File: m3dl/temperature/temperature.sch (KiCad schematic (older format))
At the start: 60 parts

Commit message: Completed all Schematics
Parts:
- removed C? (x9): 10n, symbol C_Small
- removed C? (x9): 1n, symbol C_Small
- removed J?: NORTH TOP, agg:TFML-110-02-L-D, symbol CONN_02x10
- removed J?: NORTH BOT, agg:SFML-110-02-L-D-LC, symbol CONN_02x10
- added J?: NORTH TOP, agg:TFML-110-02-L-D, symbol CONN_02x10
- added J?: NORTH BOT, agg:SFML-110-02-L-D-LC, symbol CONN_02x10
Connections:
- net CH1+: now also IC?.17 (CH2); no longer IC?.16 (CH1)
- net CH2+: now also IC?.19 (CH4); no longer IC?.18 (CH3)
- net CH3+: now also IC?.21 (CH6); no longer IC?.20 (CH5)
- net CH4+: now also IC?.23 (CH8); no longer IC?.22 (CH7)
- net CH5+: now also IC?.25 (CH10); no longer IC?.24 (CH9)
- net CH6+: now also IC?.27 (CH12); no longer IC?.26 (CH11)
- net CH7+: now also IC?.29 (CH14); no longer IC?.28 (CH13)
- net CH8+: now also IC?.31 (CH16); no longer IC?.30 (CH15)
- net CH9+: now also IC?.33 (CH18); no longer IC?.32 (CH17)
- net GND: now also IC?.16 (CH1), IC?.18 (CH3), IC?.20 (CH5), IC?.22 (CH7), IC?.24 (CH9), IC?.26 (CH11), IC?.28 (CH13), IC?.30 (CH15), IC?.32 (CH17), R?.1, R?.1, R?.1, R?.1, R?.1, R?.1, R?.1, R?.1, R?.1, J?.1, J?.1, J?.19, J?.19, J?.2, J?.2, J?.20, J?.20
- net PRESSURE1: now also J?.16, J?.16
- net PRESSURE2: now also J?.18, J?.18
- net PRESSURE3: now also J?.17, J?.17
- net SPI1_CS: now also J?.3, J?.3
- net SPI1_MISO: now also J?.13, J?.13
- net SPI1_MOSI: now also J?.11, J?.11
- net SPI1_SCK: now also J?.15, J?.15
- net STRAIN1: now also J?.4, J?.4
- net STRAIN2: now also J?.6, J?.6
- net STRAIN3: now also J?.8, J?.8
- net STRAIN4: now also J?.10, J?.10
- net STRAIN5: now also J?.12, J?.12
- net STRAIN6: now also J?.14, J?.14
- net TEMP_INT: now also J?.5, J?.5
- removed net CH1-: IC?.17 (CH2), R?.1
- removed net CH2-: IC?.19 (CH4), R?.1
- removed net CH3-: IC?.21 (CH6), R?.1
- removed net CH4-: IC?.23 (CH8), R?.1
- removed net CH5-: IC?.25 (CH10), R?.1
- removed net CH6-: IC?.27 (CH12), R?.1
- removed net CH7-: IC?.29 (CH14), R?.1
- removed net CH8-: IC?.31 (CH16), R?.1
- removed net CH9-: IC?.33 (CH18), R?.1
- new net PRESSURE4: J?.9, J?.9
- new net PRESSURE5: J?.7, J?.7
- no-connect marks 2 -> 1

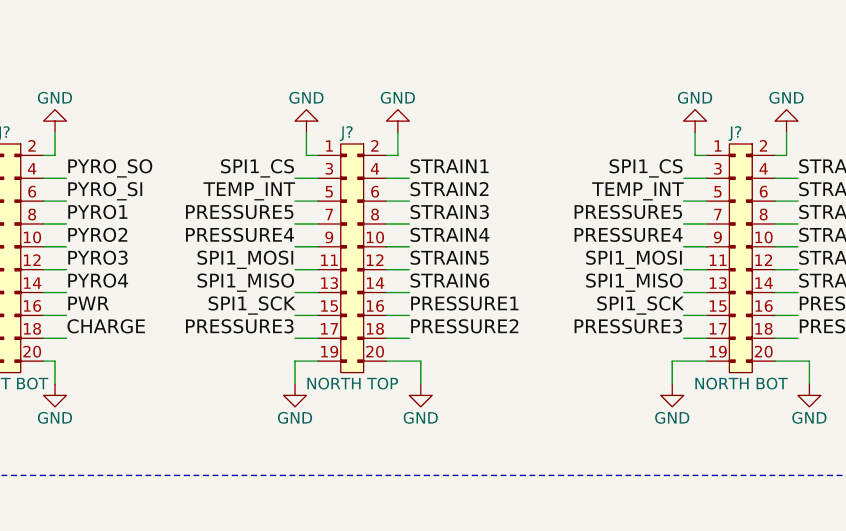
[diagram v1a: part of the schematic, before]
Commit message: Modified South Pin Header Layout
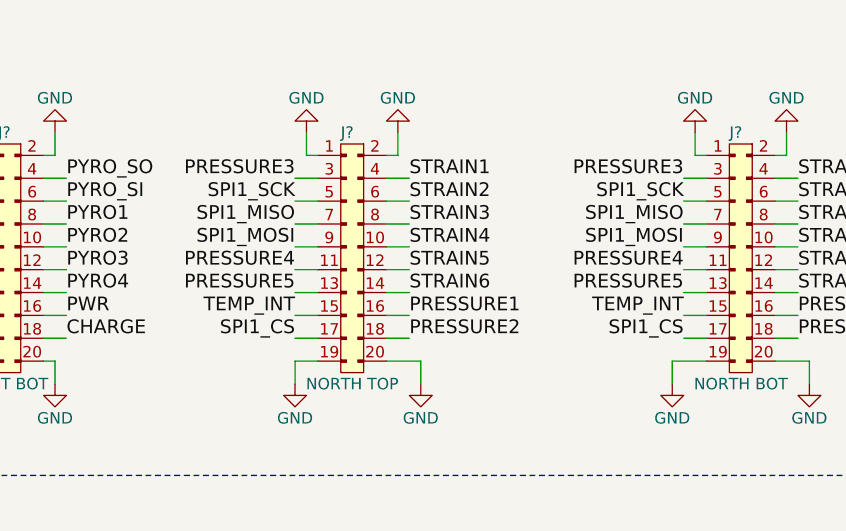
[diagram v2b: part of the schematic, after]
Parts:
- removed J?: NORTH TOP, agg:TFML-110-02-L-D, symbol CONN_02x10
- removed J?: NORTH BOT, agg:SFML-110-02-L-D-LC, symbol CONN_02x10
- added J?: NORTH TOP, agg:TFML-110-02-L-D, symbol CONN_02x10
- added J?: NORTH BOT, agg:SFML-110-02-L-D-LC, symbol CONN_02x10
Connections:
- net GND: now also J?.1, J?.1, J?.19, J?.19, J?.2, J?.2, J?.20, J?.20
- net PRESSURE1: now also J?.16, J?.16
- net PRESSURE2: now also J?.18, J?.18
- net PRESSURE3: now also J?.3, J?.3
- net PRESSURE4: now also J?.11, J?.11
- net PRESSURE5: now also J?.13, J?.13
- net SPI1_CS: now also J?.17, J?.17
- net SPI1_MISO: now also J?.7, J?.7
- net SPI1_MOSI: now also J?.9, J?.9
- net SPI1_SCK: now also J?.5, J?.5
- net STRAIN1: now also J?.4, J?.4
- net STRAIN2: now also J?.6, J?.6
- net STRAIN3: now also J?.8, J?.8
- net STRAIN4: now also J?.10, J?.10
- net STRAIN5: now also J?.12, J?.12
- net STRAIN6: now also J?.14, J?.14
- net TEMP_INT: now also J?.15, J?.15

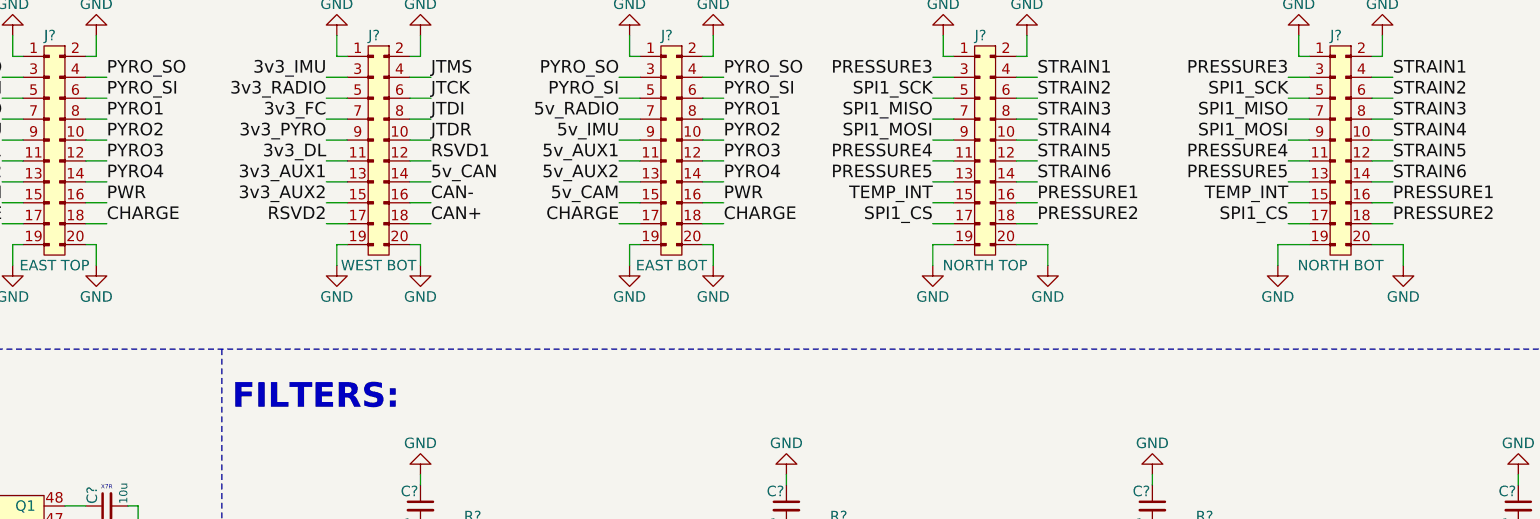
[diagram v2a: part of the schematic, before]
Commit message: Finished routing Pressure PCB - Needs Silkscreen
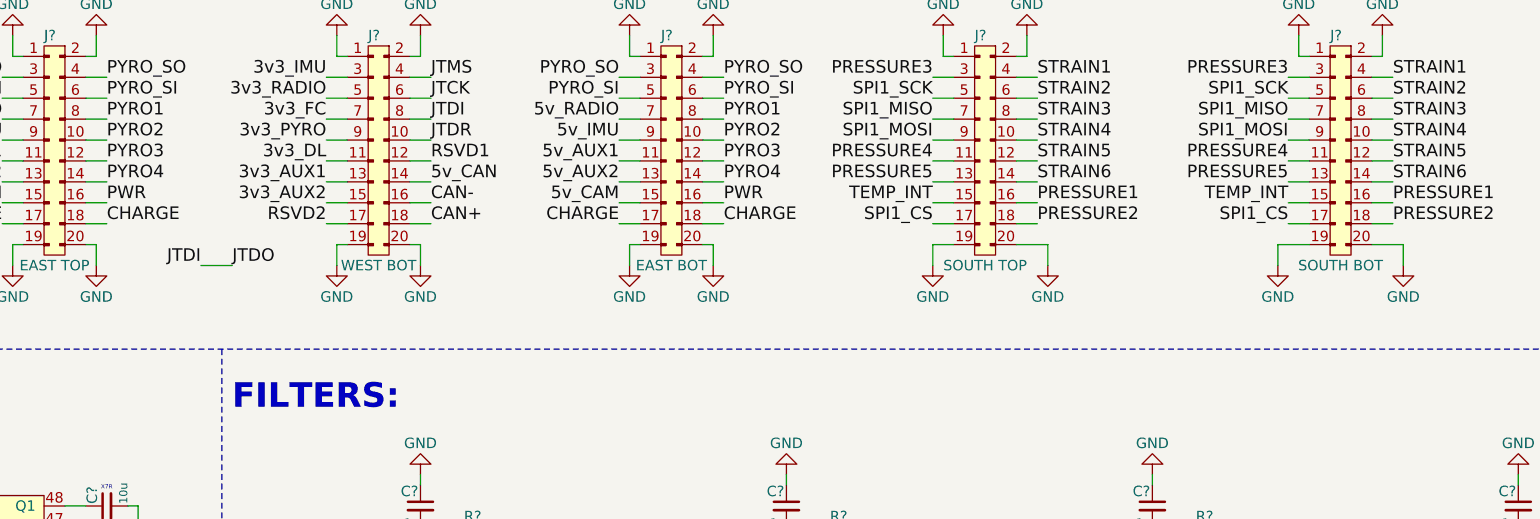
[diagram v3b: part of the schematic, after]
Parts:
- J?: value NORTH TOP -> SOUTH TOP
- J?: value NORTH BOT -> SOUTH BOT
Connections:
- net JTDO is gone; now on net JTDI: J?.8
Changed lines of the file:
@@
 P 7250 1200
 F 0 "J?" H 7150 1300 50  0000 L CNN
-F 1 "NORTH TOP" H 7200 200 50  0000 C CNN
+F 1 "SOUTH TOP" H 7200 200 50  0000 C CNN
 F 2 "agg:TFML-110-02-L-D" H 7250 1200 50  0001 C CNN
 F 3 "" H 7250 1200 50  0001 C CNN
@@
 P 8950 1200
 F 0 "J?" H 8850 1300 50  0000 L CNN
-F 1 "NORTH BOT" H 8900 200 50  0000 C CNN
+F 1 "SOUTH BOT" H 8900 200 50  0000 C CNN
 F 2 "agg:SFML-110-02-L-D-LC" H 8950 1200 50  0001 C CNN
 F 3 "" H 8950 1200 50  0001 C CNN
@@
 Text Label 6950 1800 2    60   ~ 0
 PRESSURE5
+Text Label 3600 2200 0    60   ~ 0
+JTDO
+Text Label 3450 2200 2    60   ~ 0
+JTDI
+Wire Wire Line
+	3450 2200 3600 2200
 $EndSCHEMATC

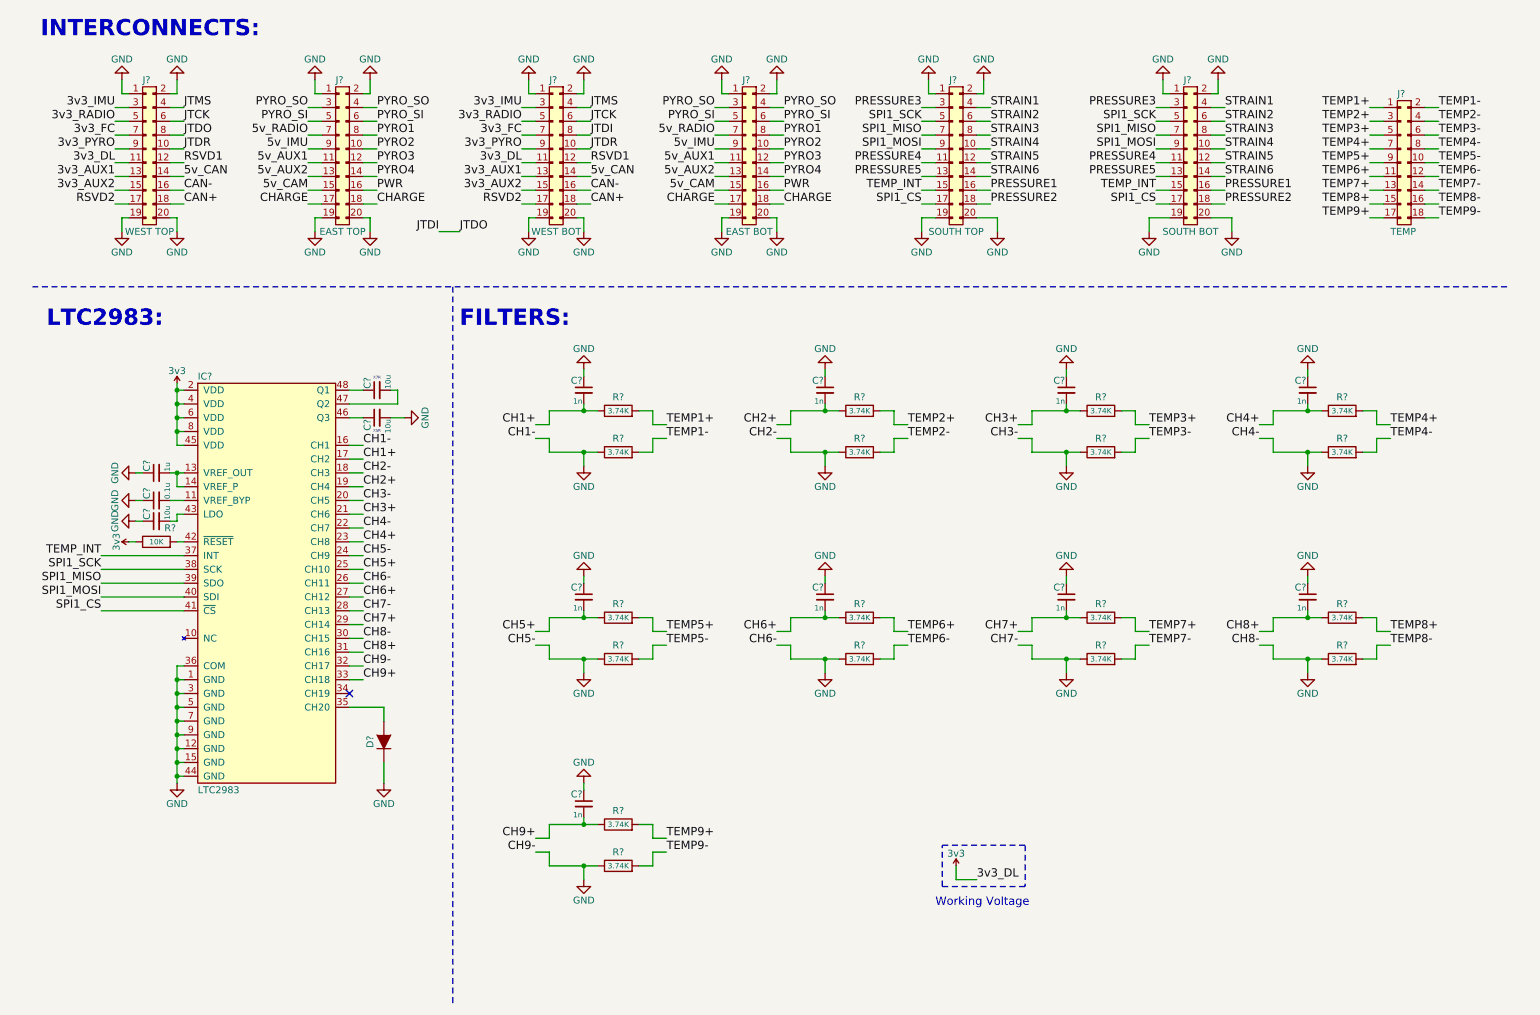
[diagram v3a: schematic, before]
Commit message: Finished Routing Temperature Board - Needs Silkscreen
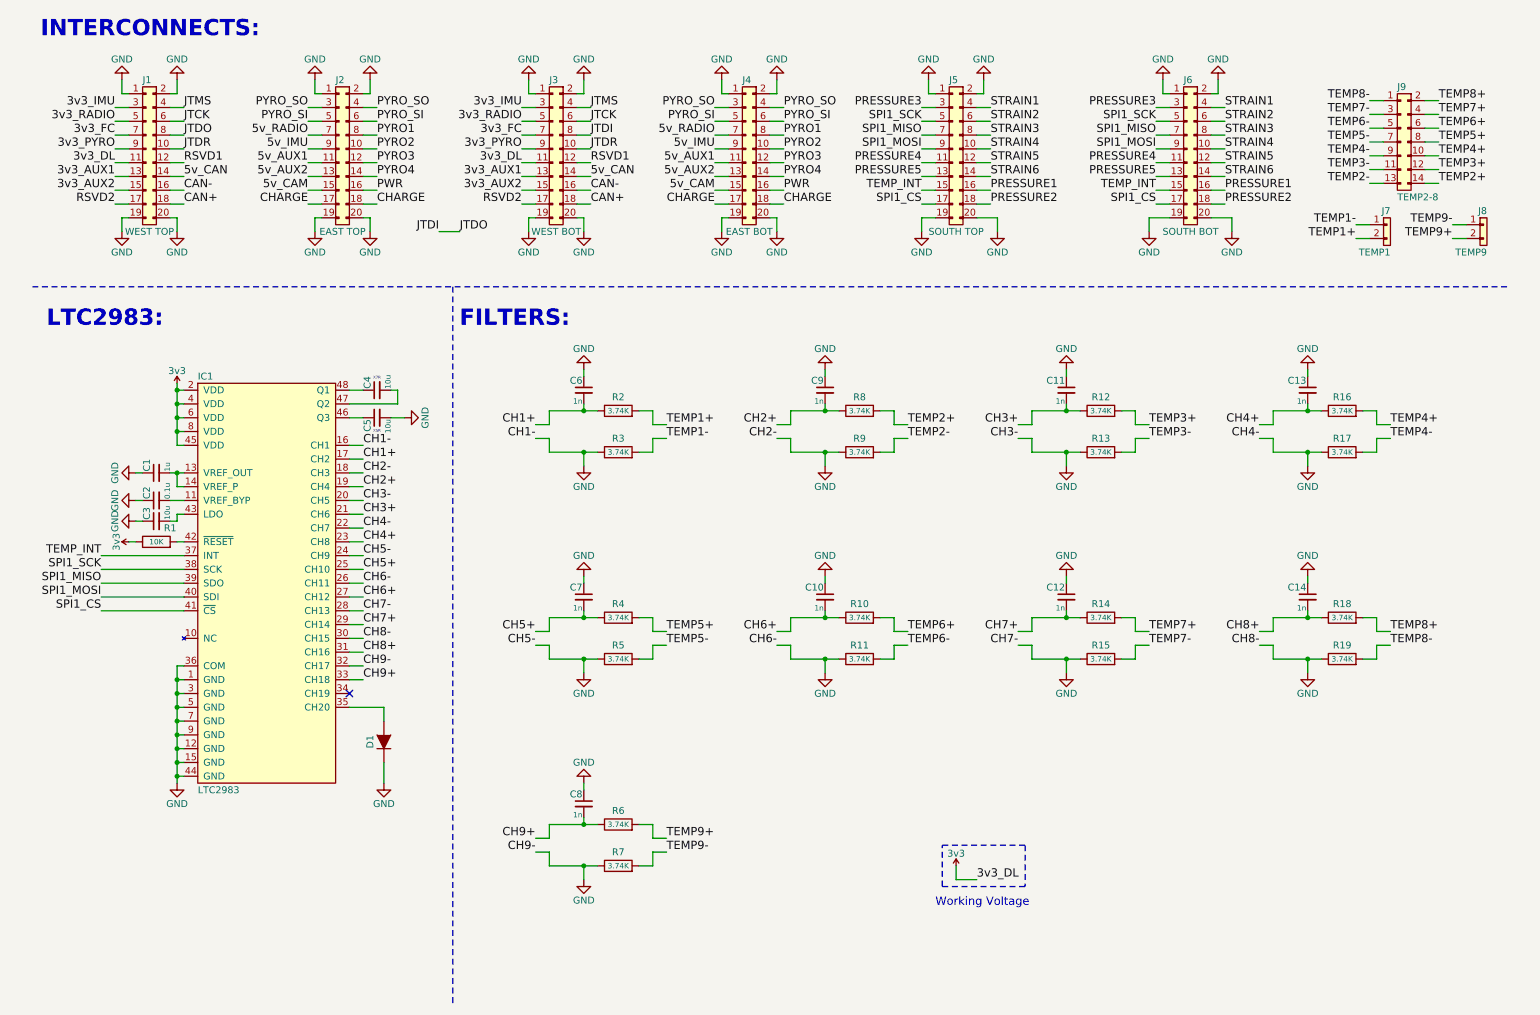
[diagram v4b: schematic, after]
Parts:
- removed J?: TEMP, symbol CONN_02x09
- added J7: TEMP1, Connectors_Molex:Connector_Molex_PicoBlade_53048-0210, symbol CONN_01x02
- added J8: TEMP9, Connectors_Molex:Connector_Molex_PicoBlade_53048-0210, symbol CONN_01x02
- added J9: TEMP2-8, Connectors_Molex:Connector_Molex_PicoBlade_53048-1410, symbol CONN_02x07
- C1, C10, C11, C12, C13, C14, C2, C3, C4, C5, C6, C7, C8, C9: renamed from C?; footprint (none) -> Capacitors_SMD:C_0603
- D1: renamed from D?; footprint (none) -> Diodes_SMD:SOD-123
- IC1: renamed from IC?; footprint LQFP-48 -> agg:LQFP-48
- R1, R10, R11, R12, R13, R14, R15, R16, R17, R18, R19, R2, R3, R4, R5, R6, R7, R8, R9: renamed from R?; footprint (none) -> Resistors_SMD:R_0603
- gave numbers to parts that had none: 6
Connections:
- net TEMP1+: now also J7.2
- net TEMP1-: now also J7.1
- net TEMP2+: now also J9.14
- net TEMP2-: now also J9.13
- net TEMP3+: now also J9.12
- net TEMP3-: now also J9.11
- net TEMP4+: now also J9.10
- net TEMP4-: now also J9.9
- net TEMP5+: now also J9.8
- net TEMP5-: now also J9.7
- net TEMP6+: now also J9.6
- net TEMP6-: now also J9.5
- net TEMP7+: now also J9.4
- net TEMP7-: now also J9.3
- net TEMP8+: now also J9.2
- net TEMP8-: now also J9.1
- net TEMP9+: now also J8.2
- net TEMP9-: now also J8.1

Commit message: Modifications as per review document
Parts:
- added C15: 100n, Capacitors_SMD:C_0603, symbol C_Small
- C2: value 0.1u -> 100n
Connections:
- net 3v3: now also C15.1
- net GND: now also C15.2

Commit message: Compiled BOM
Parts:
- C1: Farnell (none) -> 1865556
- C10, C11, C12, C13, C14, C6, C7, C8, C9: Farnell (none) -> 1813443
- C15, C2: Farnell (none) -> 2496834
- C3, C5: Farnell (none) -> 2211164
- C4: footprint Capacitors_SMD:C_0603 -> agg:0805; Farnell (none) -> 1657936
- D1: Farnell (none) -> 1773476
- J7, J8: Farnell (none) -> 1012259
- J9: Farnell (none) -> 614890
- R1: Farnell (none) -> 9238603
- R10, R11, R12, R13, R14, R15, R16, R17, R18, R19, R2, R3, R4, R5, R6, R7, R8, R9: Farnell (none) -> 2059366

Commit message: Final Tweaks before manufacture
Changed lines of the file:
@@
 L 3v3 #PWR017
 U 1 1 56B8C45F
-P 10600 6800
-F 0 "#PWR017" H 10600 6910 50  0001 L CNN
-F 1 "3v3" H 10600 6890 50  0000 C CNN
-F 2 "" H 10600 6800 60  0000 C CNN
-F 3 "" H 10600 6800 60  0000 C CNN
-	1    10600 6800
+P 10400 6800
+F 0 "#PWR017" H 10400 6910 50  0001 L CNN
+F 1 "3v3" H 10400 6890 50  0000 C CNN
+F 2 "" H 10400 6800 60  0000 C CNN
+F 3 "" H 10400 6800 60  0000 C CNN
+	1    10400 6800
 	1    0    0    -1
 $EndComp
 Text Label 10750 6900 0    60   ~ 0
 3v3_DL
-Text Notes 10450 7100 0    60   ~ 0
+Text Notes 10350 7100 0    60   ~ 0
 Working Voltage
 $Comp
@@
 Connection ~ 1550 5550
 Wire Wire Line
-	1600 5550 1550 5550
+	1550 5550 1600 5550
 Connection ~ 1550 5650
 Wire Wire Line
-	1600 5650 1550 5650
+	1550 5650 1600 5650
 Connection ~ 1550 5750
 Wire Wire Line
-	1600 5750 1550 5750
+	1550 5750 1600 5750
 Connection ~ 1550 5850
 Wire Wire Line
-	1600 5850 1550 5850
+	1550 5850 1600 5850
 Connection ~ 1550 5950
 Wire Wire Line
-	1600 5950 1550 5950
+	1550 5950 1600 5950
 Connection ~ 1550 6050
 Wire Wire Line
-	1600 6050 1550 6050
+	1550 6050 1600 6050
 Connection ~ 1550 6150
-Wire Wire Line
-	1500 6150 1600 6150
 Wire Wire Line
 	1550 5350 1550 6200
@@
 Connection ~ 1550 3350
 Wire Wire Line
-	1500 3350 1600 3350
+	1550 3350 1600 3350
 Connection ~ 1550 3450
 Wire Wire Line
@@
 Connection ~ 1550 3550
 Wire Wire Line
-	1600 3550 1550 3550
+	1550 3550 1600 3550
 Connection ~ 1550 3650
 Wire Wire Line
-	1600 3650 1550 3650
+	1550 3650 1600 3650
 Wire Wire Line
 	1550 3750 1600 3750
@@
 	1550 3300 1550 3750
 Wire Notes Line
-	10500 6650 11100 6650
+	10300 6650 11100 6650
 Wire Notes Line
-	10500 6950 10500 6650
+	10300 6950 11100 6950
 Wire Notes Line
-	11100 6950 10500 6950
-Wire Notes Line
-	11100 6650 11100 6950
-Wire Wire Line
-	10600 6900 10750 6900
-Wire Wire Line
-	10600 6800 10600 6900
+	11100 6950 11100 6650
+Wire Wire Line
+	10400 6900 10750 6900
+Wire Wire Line
+	10400 6800 10400 6900
 Wire Wire Line
 	1150 1100 1150 1200
@@
 	1550 2100 1550 2200
 Wire Wire Line
-	1200 2100 1150 2100
+	1100 2100 1200 2100
 Wire Wire Line
 	1150 2100 1150 2200
@@
 L PWR #FLG052
 U 1 1 575C61DD
-P 1500 3350
-F 0 "#FLG052" H 1500 3510 50  0001 C CNN
-F 1 "PWR" H 1500 3440 50  0000 C CNN
-F 2 "" H 1500 3350 50  0001 C CNN
-F 3 "" H 1500 3350 50  0001 C CNN
-	1    1500 3350
-	0    -1   -1   0
+P 10600 6850
+F 0 "#FLG052" H 10600 7010 50  0001 C CNN
+F 1 "PWR" H 10600 6940 50  0000 C CNN
+F 2 "" H 10600 6850 50  0001 C CNN
+F 3 "" H 10600 6850 50  0001 C CNN
+	1    10600 6850
+	1    0    0    -1
 $EndComp
 $Comp
 L PWR #FLG053
 U 1 1 575C6A06
-P 1500 6150
-F 0 "#FLG053" H 1500 6310 50  0001 C CNN
-F 1 "PWR" H 1500 6240 50  0000 C CNN
-F 2 "" H 1500 6150 50  0001 C CNN
-F 3 "" H 1500 6150 50  0001 C CNN
-	1    1500 6150
+P 1100 2100
+F 0 "#FLG053" H 1100 2260 50  0001 C CNN
+F 1 "PWR" H 1100 2190 50  0000 C CNN
+F 2 "" H 1100 2100 50  0001 C CNN
+F 3 "" H 1100 2100 50  0001 C CNN
+	1    1100 2100
 	0    -1   -1   0
 $EndComp
@@
 	0    -1   -1   0
 $EndComp
+Wire Wire Line
+	10600 6850 10600 6900
+Connection ~ 10600 6900
+Wire Notes Line
+	10300 6950 10300 6650
+Wire Wire Line
+	1550 6150 1600 6150
+Connection ~ 1150 2100
 $EndSCHEMATC

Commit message: Final tweaks
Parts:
- IC1: Digikey (none) -> LTC2983ILX#PBF-ND; Farnell 2461149 -> (none)
- J9: Digikey (none) -> WM17007-ND; Farnell 614890 -> (none)
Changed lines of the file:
@@
 F 2 "agg:LQFP-48" H 1700 3150 50  0001 L CNN
 F 3 "http://cds.linear.com/docs/en/datasheet/2983fc.pdf" H 1700 3050 50  0001 L CNN
-F 4 "2461149" H 1700 2950 50  0001 L CNN "Farnell"
+F 4 "LTC2983ILX#PBF-ND " H 1700 2950 50  0001 L CNN "Digikey"
 	1    2200 4750
 	1    0    0    -1
@@
 F 2 "Connectors_Molex:Connector_Molex_PicoBlade_53048-1410" H 10500 1250 50  0001 C CNN
 F 3 "" H 10500 1250 50  0001 C CNN
-F 4 "614890" H 10500 1250 60  0001 C CNN "Farnell"
+F 4 "WM17007-ND " H 10500 1250 60  0001 C CNN "Digikey"
 	1    10500 1250
 	1    0    0    -1
